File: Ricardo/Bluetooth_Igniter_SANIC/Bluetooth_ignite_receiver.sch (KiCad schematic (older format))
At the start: 1 part

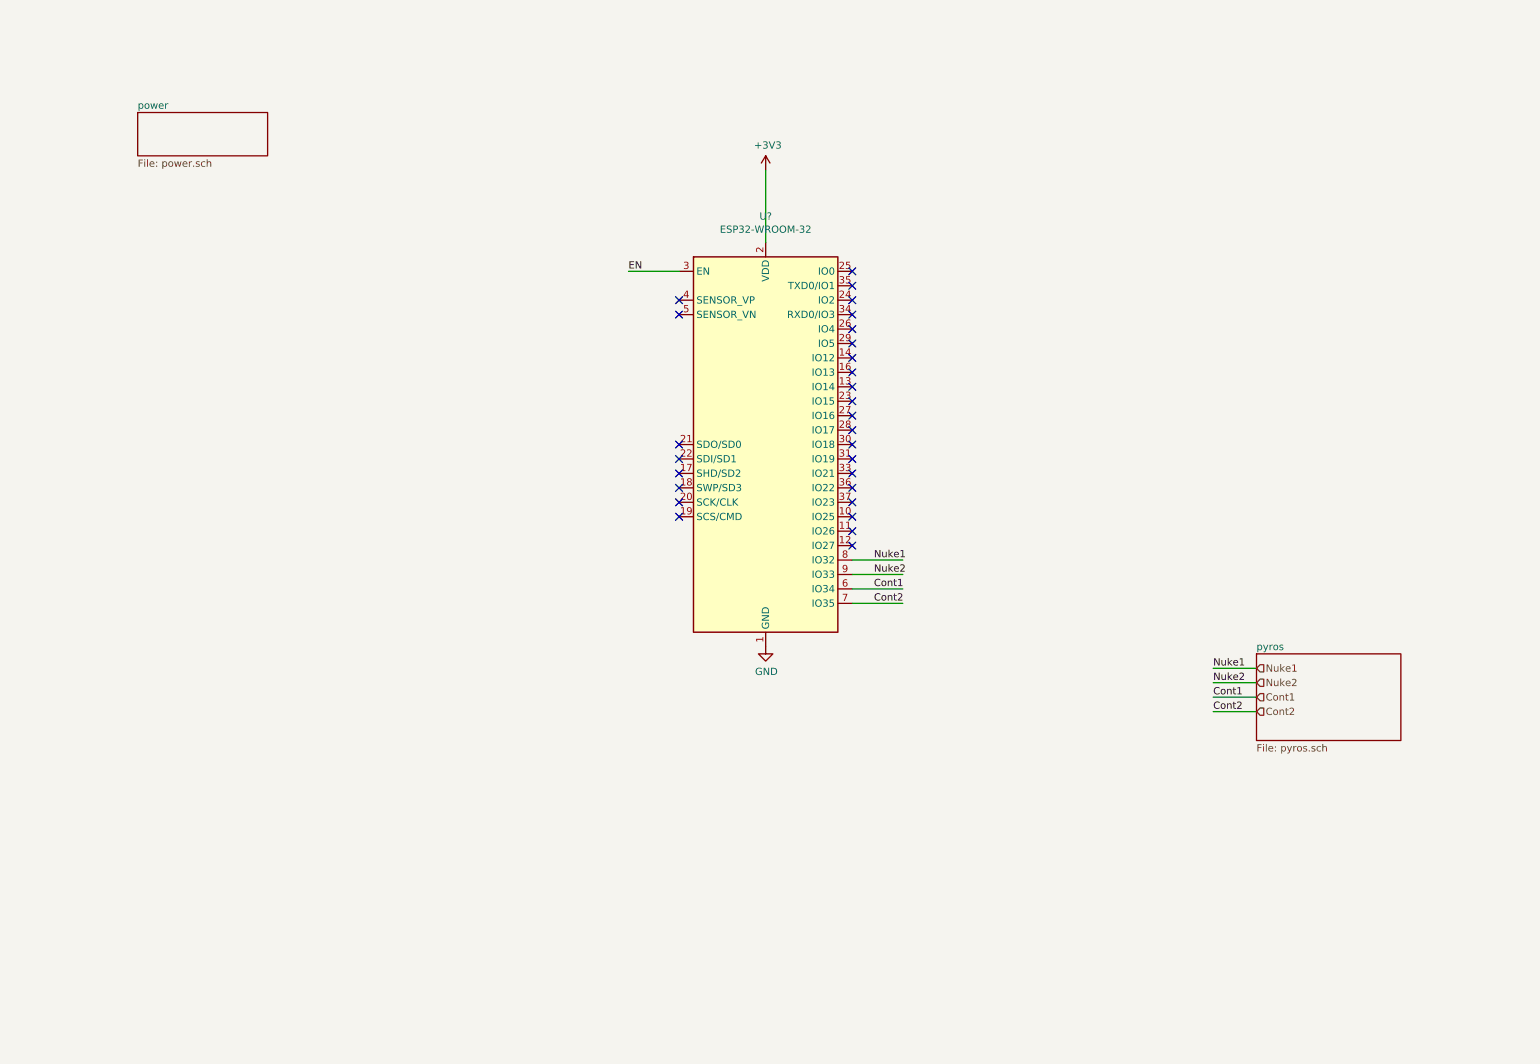
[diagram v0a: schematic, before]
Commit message: updated
sized voltage regulator components
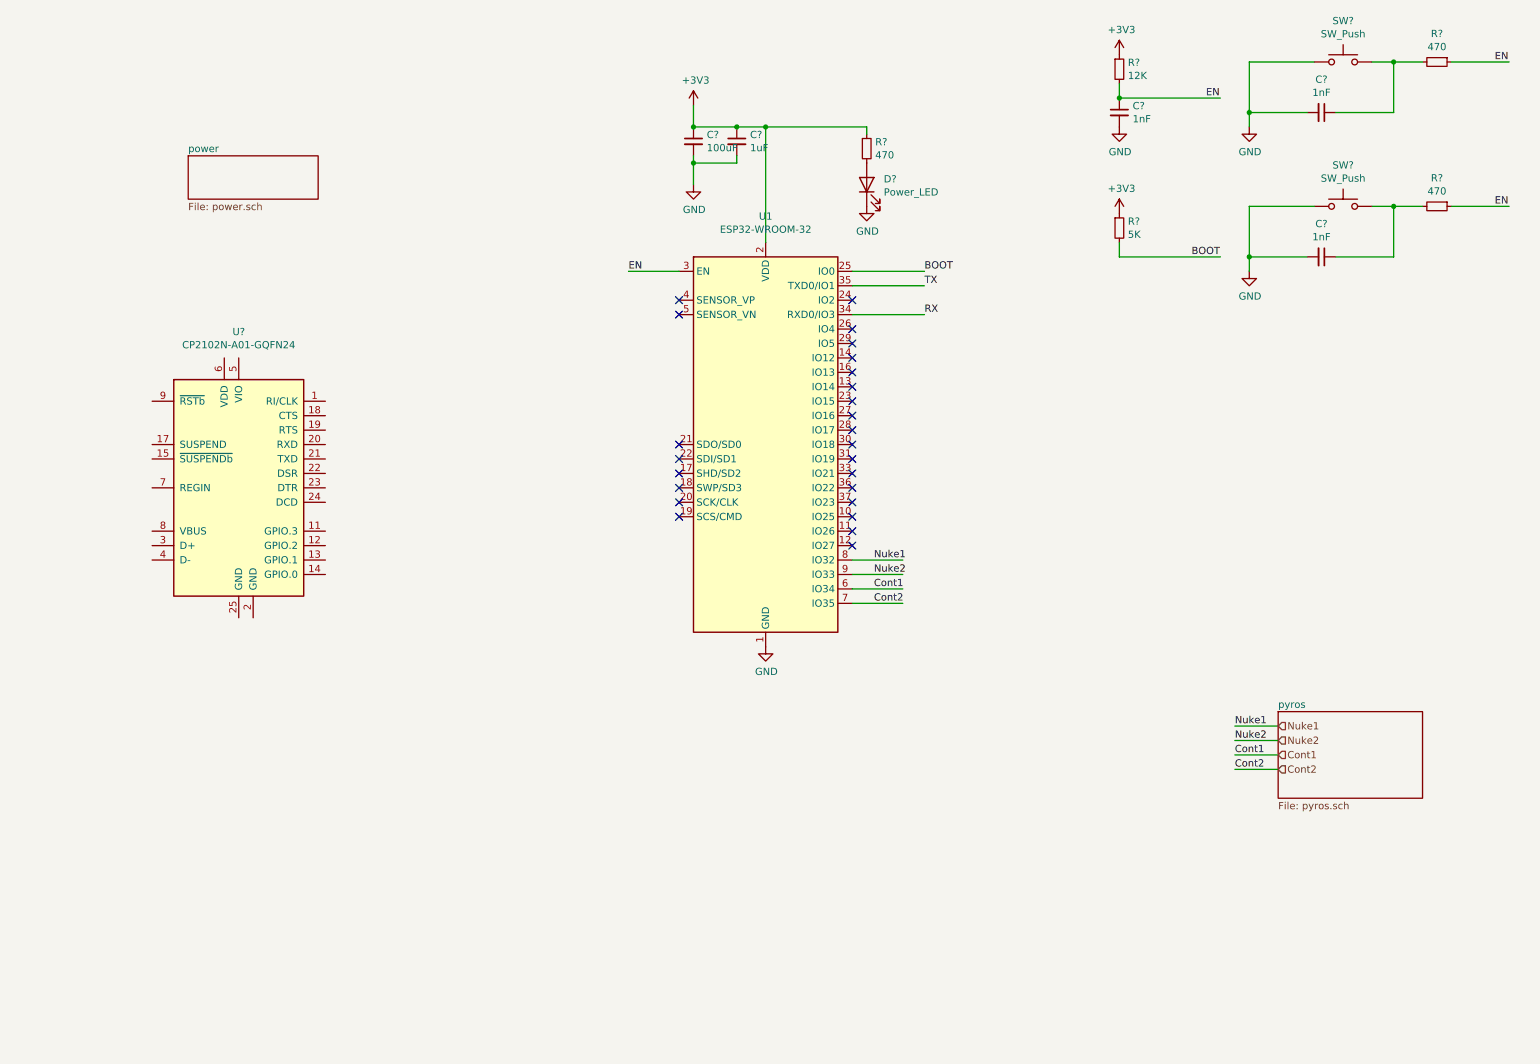
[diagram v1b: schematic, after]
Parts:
- added C?: 100uF, symbol Device:C_Small
- added C?: 1uF, symbol Device:C_Small
- added C? (x3): 1nF, symbol Device:C_Small
- added D?: Power_LED, symbol Device:LED
- added R? (x3): 470, symbol Device:R_Small
- added R?: 12K, symbol Device:R_Small
- added R?: 5K, symbol Device:R_Small
- added SW? (x2): SW_Push, symbol Switch:SW_Push
- added U?: CP2102N-A01-GQFN24, Package_DFN_QFN:QFN-24-1EP_4x4mm_P0.5mm_EP2.6x2.6mm, symbol Interface_USB:CP2102N-A01-GQFN24
- gave numbers to parts that had none: 1
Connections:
- net labels added: BOOT, RX, TX
- wire segments 10 -> 44
- no-connect marks 28 -> 25

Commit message: Added USB
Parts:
- added D?: D_Schottky, symbol Device:D_Schottky
- added D?: SP0503BAHT, Package_TO_SOT_SMD:SOT-143, symbol Power_Protection:SP0503BAHT
- added Q? (x2): MMDT2222A, Package_TO_SOT_SMD:SOT-363_SC-70-6, symbol Transistor_BJT:MMDT2222A
- added R?: 1K, symbol Device:R_Small
- added R?: 22K, symbol Device:R_Small
- added R?: 43K, symbol Device:R_Small
- added R? (x2): 10K, symbol Device:R_Small
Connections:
- net labels added: D+, D-, DTR, RTS, RXD, TXD, VBUS, VDD
- net labels removed: RX, TX
- wire segments 44 -> 91
- no-connect marks 25 -> 35
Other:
- moved on the sheet: U?

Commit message: Finished schematic; starting pcb design
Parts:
- C1, C2, C3, C4, C5: renamed from C?; footprint (none) -> Capacitor_SMD:C_0603_1608Metric
- D1: renamed from D?; footprint (none) -> Diode_SMD:D_SOD-123F
- D3: renamed from D?; footprint (none) -> LED_SMD:LED_0603_1608Metric_Castellated
- R1, R10, R2, R3, R4, R5, R6, R7, R8, R9: renamed from R?; footprint (none) -> Resistor_SMD:R_0603_1608Metric
- gave numbers to parts that had none: 6
- renumbered U1 to U2
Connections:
- net labels removed: D+, D-, VBUS
